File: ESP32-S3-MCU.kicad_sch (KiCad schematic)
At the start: 29 parts, among them SW1 RESET, SW2 BOOT, U1 ESP32-S3FH4R2, Y1 Crystal_GND24_Small

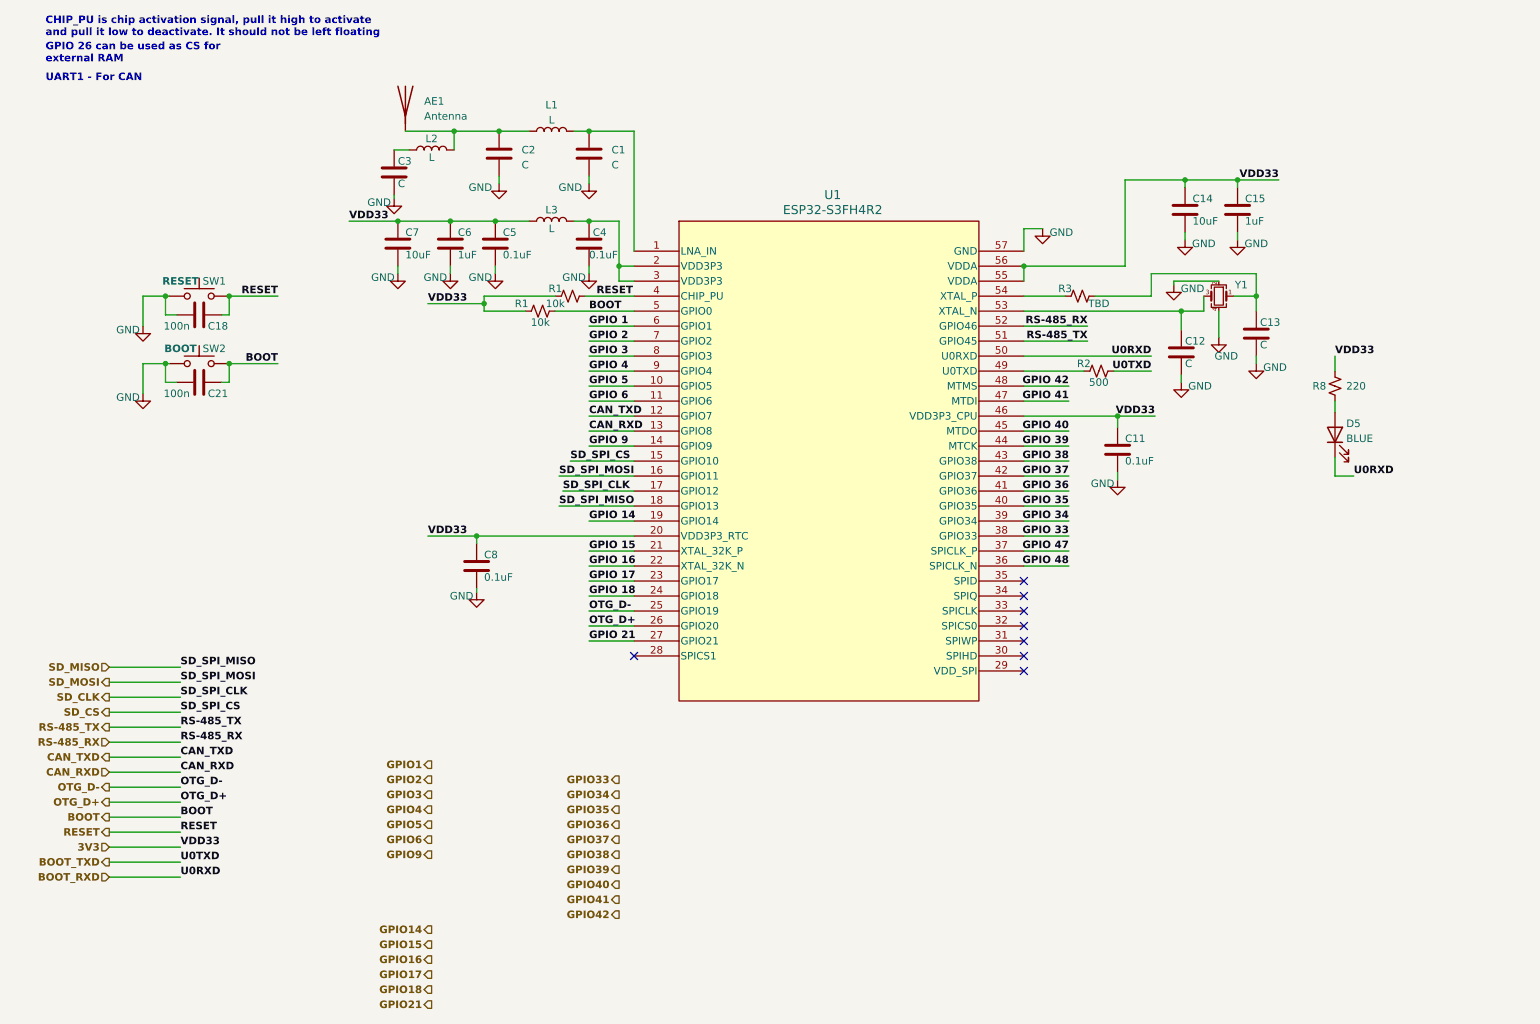
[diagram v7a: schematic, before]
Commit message: Added Female Headers
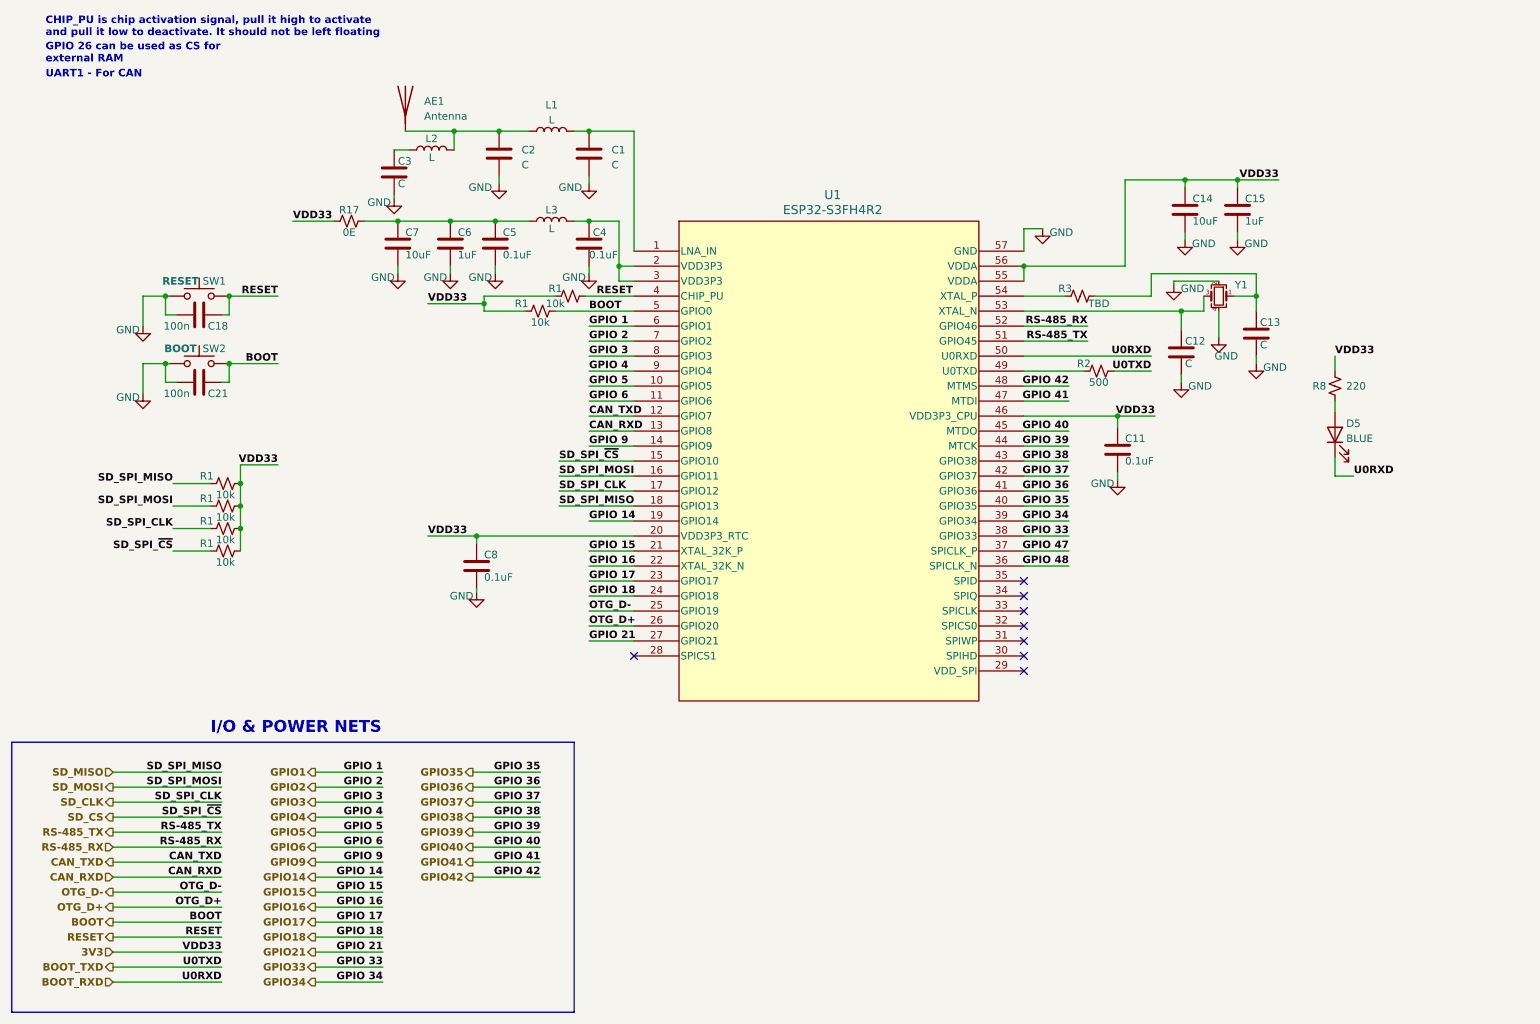
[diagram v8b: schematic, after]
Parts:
- added R1 (x4): 10k, symbol ESP32-S3_DB:R_Small_US
- added R17: 0E, symbol ESP32-S3_DB:R_Small_US
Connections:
- net GPIO 1 is gone; now on net GPIO1: U1.6 (GPIO1)
- net GPIO 14 is gone; now on net GPIO14: U1.19 (GPIO14)
- net GPIO 15 is gone; now on net GPIO15: U1.21 (XTAL_32K_P)
- net GPIO 16 is gone; now on net GPIO16: U1.22 (XTAL_32K_N)
- net GPIO 17 is gone; now on net GPIO17: U1.23 (GPIO17)
- net GPIO 18 is gone; now on net GPIO18: U1.24 (GPIO18)
- net GPIO 2 is gone; now on net GPIO2: U1.7 (GPIO2)
- net GPIO 21 is gone; now on net GPIO21: U1.27 (GPIO21)
- net GPIO 3 is gone; now on net GPIO3: U1.8 (GPIO3)
- net GPIO 33 is gone; now on net GPIO33: U1.38 (GPIO33)
- net GPIO 34 is gone; now on net GPIO34: U1.39 (GPIO34)
- net GPIO 35 is gone; now on net GPIO35: U1.40 (GPIO35)
- net GPIO 36 is gone; now on net GPIO36: U1.41 (GPIO36)
- net GPIO 37 is gone; now on net GPIO37: U1.42 (GPIO37)
- net GPIO 38 is gone; now on net GPIO38: U1.43 (GPIO38)
- net GPIO 39 is gone; now on net GPIO39: U1.44 (MTCK)
- net GPIO 4 is gone; now on net GPIO4: U1.9 (GPIO4)
- net GPIO 40 is gone; now on net GPIO40: U1.45 (MTDO)
- net GPIO 41 is gone; now on net GPIO41: U1.47 (MTDI)
- net GPIO 42 is gone; now on net GPIO42: U1.48 (MTMS)
- net GPIO 5 is gone; now on net GPIO5: U1.10 (GPIO5)
- net GPIO 6 is gone; now on net GPIO6: U1.11 (GPIO6)
- net GPIO 9 is gone; now on net GPIO9: U1.14 (GPIO9)
- net 3V3: now also R1.2, R1.2, R1.2, R1.2, R17.1; no longer C5.1, C6.1, C7.1, L3.1
- net SD_CLK: now also R1.1
- net SD_CS: now also R1.1
- net SD_MISO: now also R1.1
- net SD_MOSI: now also R1.1
- new net: C5.1, C6.1, C7.1, L3.1, R17.2
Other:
- note added: "I/O & POWER NETS"
